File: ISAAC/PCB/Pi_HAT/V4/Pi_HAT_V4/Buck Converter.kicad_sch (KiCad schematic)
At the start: 21 parts, among them J4 Conn_01x04_Male, J5 XT60PW-M, J6 Conn_01x04_Male, J8 XT60PW-M, U1 MP2315GJ-Z

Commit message: Updated code: Sorta works
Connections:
- net 12V renamed VCC1
- net VCC1: no longer J4.1 (Pin_1), J5.1 (+), J6.1 (Pin_1)
- new net VCC0: J4.1 (Pin_1), J5.1 (+), J6.1 (Pin_1)
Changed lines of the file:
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@@
 (kicad_sch (version 20230121) (generator eeschema)
   (paper "A4")
-  (junction (at 116.84 44.45) (diameter 0) (color 0 0 0 0)
+  (junction (at 110.49 41.91) (diameter 0) (color 0 0 0 0)
   )
   (junction (at 194.31 67.31) (diameter 0) (color 0 0 0 0)
@@
   (junction (at 87.63 81.28) (diameter 0) (color 0 0 0 0)
   )
+  (junction (at 114.3 44.45) (diameter 0) (color 0 0 0 0)
+  )
   (junction (at 173.99 92.71) (diameter 0) (color 0 0 0 0)
   )
@@
   (junction (at 182.88 67.31) (diameter 0) (color 0 0 0 0)
   )
-  (wire (pts (xy 99.06 41.91) (xy 103.632 41.91))
-    (stroke (width 0) (type default))
-  )
   (wire (pts (xy 182.88 92.71) (xy 173.99 92.71))
     (stroke (width 0) (type default))
@@
     (stroke (width 0) (type default))
   )
+  (wire (pts (xy 114.3 41.91) (xy 114.3 44.45))
+    (stroke (width 0) (type default))
+  )
   (wire (pts (xy 154.94 67.31) (xy 158.75 67.31))
     (stroke (width 0) (type default))
@@
     (stroke (width 0) (type default))
   )
+  (wire (pts (xy 114.3 44.45) (xy 116.84 44.45))
+    (stroke (width 0) (type default))
+  )
   (wire (pts (xy 166.37 67.31) (xy 170.18 67.31))
     (stroke (width 0) (type default))
@@
     (stroke (width 0) (type default))
   )
+  (wire (pts (xy 110.49 41.91) (xy 114.3 41.91))
+    (stroke (width 0) (type default))
+  )
   (wire (pts (xy 166.37 86.36) (xy 166.37 92.71))
     (stroke (width 0) (type default))
@@
     (stroke (width 0) (type default))
   )
-  (wire (pts (xy 75.438 41.148) (xy 80.01 41.148))
-    (stroke (width 0) (type default))
-  )
-  (wire (pts (xy 132.588 47.498) (xy 116.84 47.498))
+  (wire (pts (xy 83.82 35.56) (xy 110.49 35.56))
+    (stroke (width 0) (type default))
+  )
+  (wire (pts (xy 83.82 35.56) (xy 83.82 41.148))
     (stroke (width 0) (type default))
   )
@@
     (stroke (width 0) (type default))
   )
-  (wire (pts (xy 116.84 47.498) (xy 116.84 44.45))
+  (wire (pts (xy 99.06 41.91) (xy 110.49 41.91))
     (stroke (width 0) (type default))
   )
@@
     (stroke (width 0) (type default))
   )
+  (wire (pts (xy 110.49 35.56) (xy 110.49 41.91))
+    (stroke (width 0) (type default))
+  )
   (wire (pts (xy 146.05 92.71) (xy 142.24 92.71))
     (stroke (width 0) (type default))
   )
   (wire (pts (xy 153.67 92.71) (xy 166.37 92.71))
+    (stroke (width 0) (type default))
+  )
+  (wire (pts (xy 75.438 41.148) (xy 83.82 41.148))
     (stroke (width 0) (type default))
   )
@@
     (effects (font (size 2 2)) (justify left bottom))
   )
-  (label "VCC" (at 80.01 41.148 180) (fields_autoplaced)
-    (effects (font (size 1.27 1.27)) (justify right bottom))
-  )
-  (label "VCC" (at 103.632 41.91 180) (fields_autoplaced)
-    (effects (font (size 1.27 1.27)) (justify right bottom))
-  )
   (label "12V" (at 132.588 47.498 180) (fields_autoplaced)
     (effects (font (size 1.27 1.27)) (justify right bottom))
   )
-  (label "VCC" (at 121.158 47.498 0) (fields_autoplaced)
-    (effects (font (size 1.27 1.27)) (justify left bottom))
-  )
   (label "12V" (at 83.82 81.28 180) (fields_autoplaced)
     (effects (font (size 1.27 1.27)) (justify right bottom))
   )
+  (hierarchical_label "VCC0" (shape input) (at 116.84 44.45 270) (fields_autoplaced)
+    (effects (font (size 1.27 1.27)) (justify right))
+  )
   (hierarchical_label "SCL" (shape input) (at 75.438 46.228 0) (fields_autoplaced)
     (effects (font (size 1.27 1.27)) (justify left))
@@
     (effects (font (size 1.27 1.27)) (justify left))
   )
+  (hierarchical_label "VCC1" (shape input) (at 132.588 44.45 180) (fields_autoplaced)
+    (effects (font (size 1.27 1.27)) (justify right))
+  )
   (symbol (lib_id "power:GND") (at 119.38 44.45 0) (unit 1)
     (in_bom yes) (on_board yes) (dnp no)
@@
     )
     (property "Value" "GND" (at 121.92 46.99 0)
-      (effects (font (size 1.27 1.27)) hide)
+      (effects (font (size 1.27 1.27)))
     )
     (property "Footprint" "" (at 119.38 44.45 0)
@@
       (effects (font (size 1.27 1.27)) hide)
     )
-    (property "Value" "GND" (at 101.854 44.45 90)
+    (property "Value" "GND" (at 101.346 43.434 90)
       (effects (font (size 1.27 1.27)) (justify right))
     )
@@
     )
   )
-  (symbol (lib_id "power:PWR_FLAG") (at 116.84 44.45 90) (unit 1)
-    (in_bom yes) (on_board yes) (dnp no)
-    (property "Reference" "#FLG0101" (at 114.935 44.45 0)
-      (effects (font (size 1.27 1.27)) hide)
-    )
-    (property "Value" "PWR_FLAG" (at 113.284 46.482 90)
-      (effects (font (size 1.27 1.27)))
-    )
-    (property "Footprint" "" (at 116.84 44.45 0)
-      (effects (font (size 1.27 1.27)) hide)
-    )
-    (property "Datasheet" "~" (at 116.84 44.45 0)
-      (effects (font (size 1.27 1.27)) hide)
-    )
+  (symbol (lib_id "power:PWR_FLAG") (at 114.3 44.45 0) (unit 1)
+    (in_bom yes) (on_board yes) (dnp no)
+    (property "Reference" "#FLG0101" (at 114.3 42.545 0)
+      (effects (font (size 1.27 1.27)) hide)
+    )
+    (property "Value" "PWR_FLAG" (at 114.3 40.894 0)
+      (effects (font (size 1.27 1.27)))
+    )
+    (property "Footprint" "" (at 114.3 44.45 0)
+      (effects (font (size 1.27 1.27)) hide)
+    )
+    (property "Datasheet" "~" (at 114.3 44.45 0)
+      (effects (font (size 1.27 1.27)) hide)
+    )

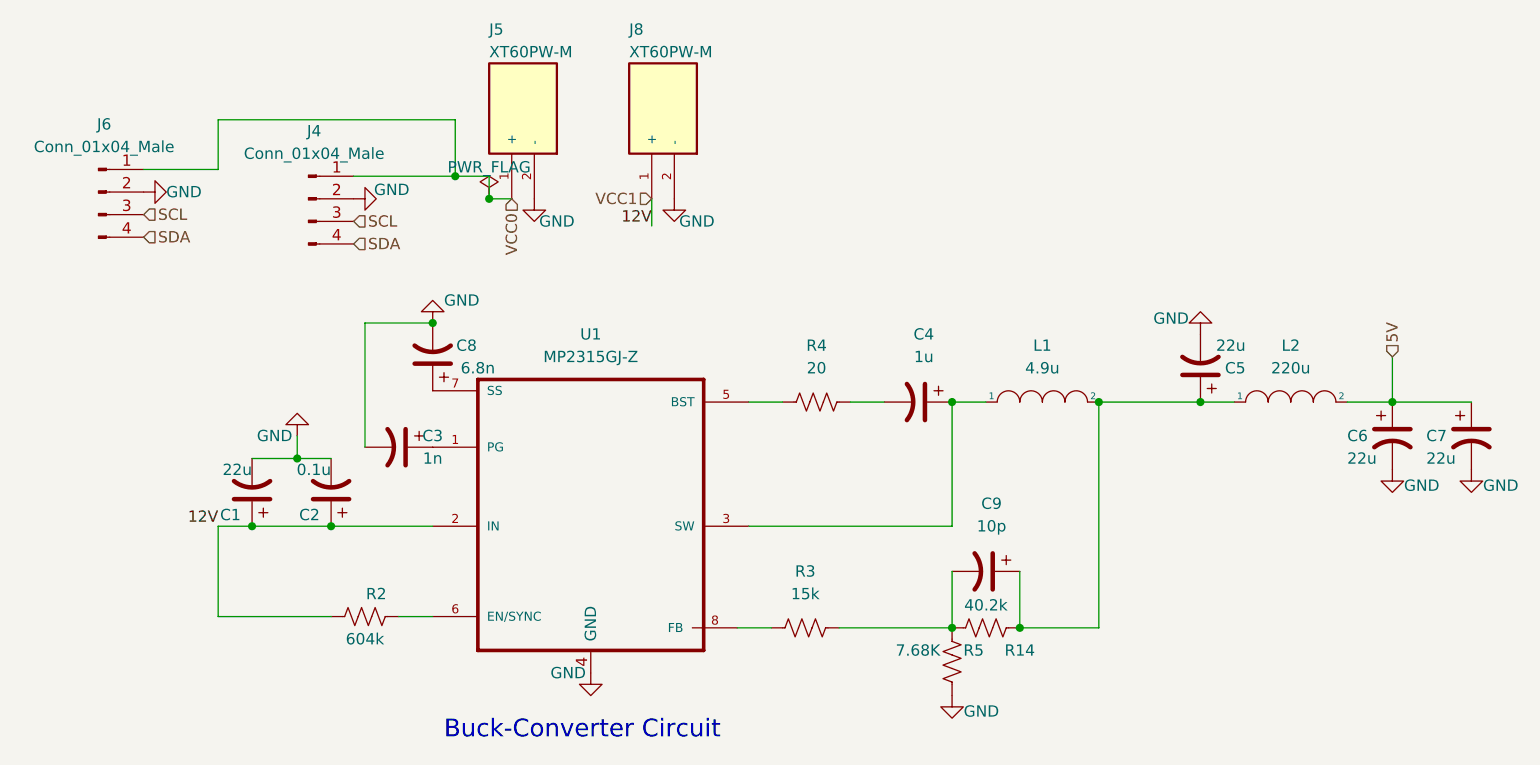
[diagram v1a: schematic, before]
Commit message: Updated
Started SPARK grant and updated controller and PCB
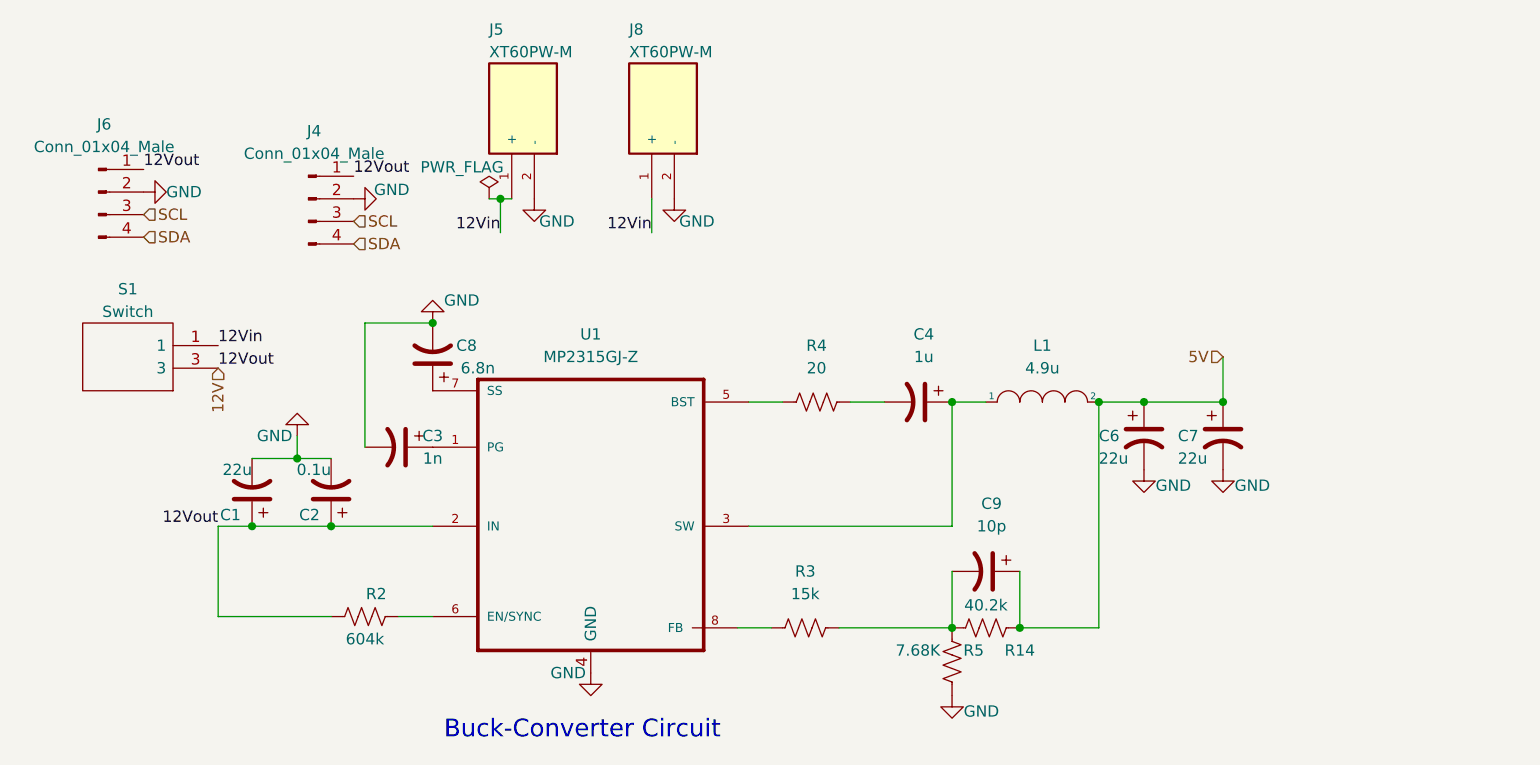
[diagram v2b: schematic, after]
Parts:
- removed C5: 22u, Capacitor_SMD:C_1210_3225Metric_Pad1.33x2.70mm_HandSolder, symbol Device:C_Polarized_US
- removed L2: 220u, .pretty:IND_AIRD-02-151K, symbol pspice:INDUCTOR
- added S1: Switch, refV:2MS6T4B3M2CES, symbol 2MS6T4B3M2CES:2MS6T4B3M2CES
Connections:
- net 5V: now also C9.1, L1.2, R14.1
- net VCC0 renamed 12V
- net 12V: now also C1.1, C2.1, R2.1, U1.2 (IN), S1.3; no longer J5.1 (+)
- removed net VCC1: C1.1, C2.1, J8.1 (+), R2.1, U1.2 (IN)
- new net 12Vin: J5.1 (+), J8.1 (+), S1.1
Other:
- moved on the sheet: C6, C7
